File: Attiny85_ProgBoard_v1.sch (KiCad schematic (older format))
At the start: 1 part

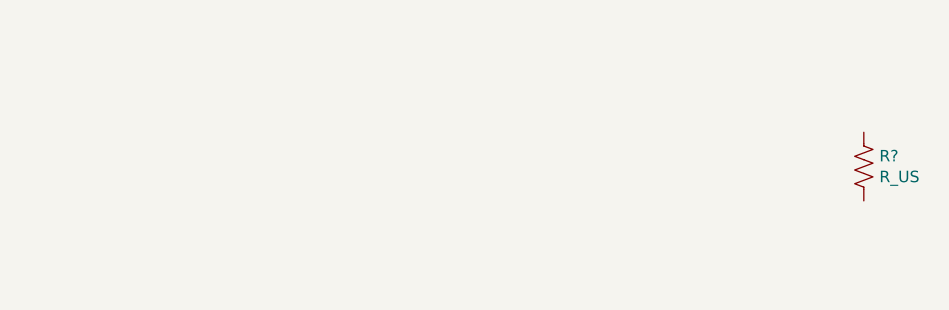
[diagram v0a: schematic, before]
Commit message: Added Attiny85 schematic symbol and footprint
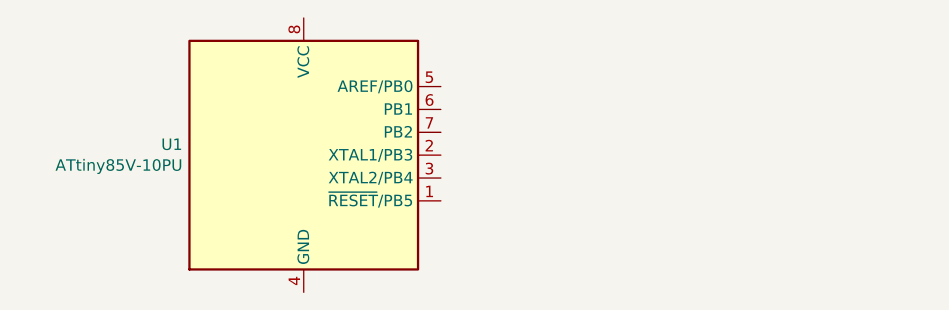
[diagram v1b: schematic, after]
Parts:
- removed R?: R_US, symbol Device:R_US
- added U1: ATtiny85V-10PU, Package_DIP:DIP-8_W7.62mm, symbol MCU_Microchip_ATtiny:ATtiny85V-10PU
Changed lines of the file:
@@
 $EndDescr
 $Comp
-L Device:R_US R?
-U 1 1 6342D2C3
-P 7200 3050
-F 0 "R?" H 7268 3096 50  0000 L CNN
-F 1 "R_US" H 7268 3005 50  0000 L CNN
-F 2 "" V 7240 3040 50  0001 C CNN
-F 3 "~" H 7200 3050 50  0001 C CNN
-	1    7200 3050
+L MCU_Microchip_ATtiny:ATtiny85V-10PU U1
+U 1 1 6345C714
+P 4750 3000
+F 0 "U1" H 4220 3046 50  0000 R CNN
+F 1 "ATtiny85V-10PU" H 4220 2955 50  0000 R CNN
+F 2 "Package_DIP:DIP-8_W7.62mm" H 4750 3000 50  0001 C CIN
+F 3 "http://ww1.microchip.com/downloads/en/DeviceDoc/atmel-2586-avr-8-bit-microcontroller-attiny25-attiny45-attiny85_datasheet.pdf" H 4750 3000 50  0001 C CNN
+	1    4750 3000
 	1    0    0    -1
 $EndComp
